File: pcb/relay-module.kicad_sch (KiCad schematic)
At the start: 57 parts, among them J1 AVR-UPDI-6, J2 QWICC, J3 Power In, J4 Power Out, K1 PR24-5V-900-1A, P1 MountingHole_Pad, P2 MountingHole_Pad, P3 MountingHole_Pad, P4 MountingHole_Pad, Q1 MMBT3904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

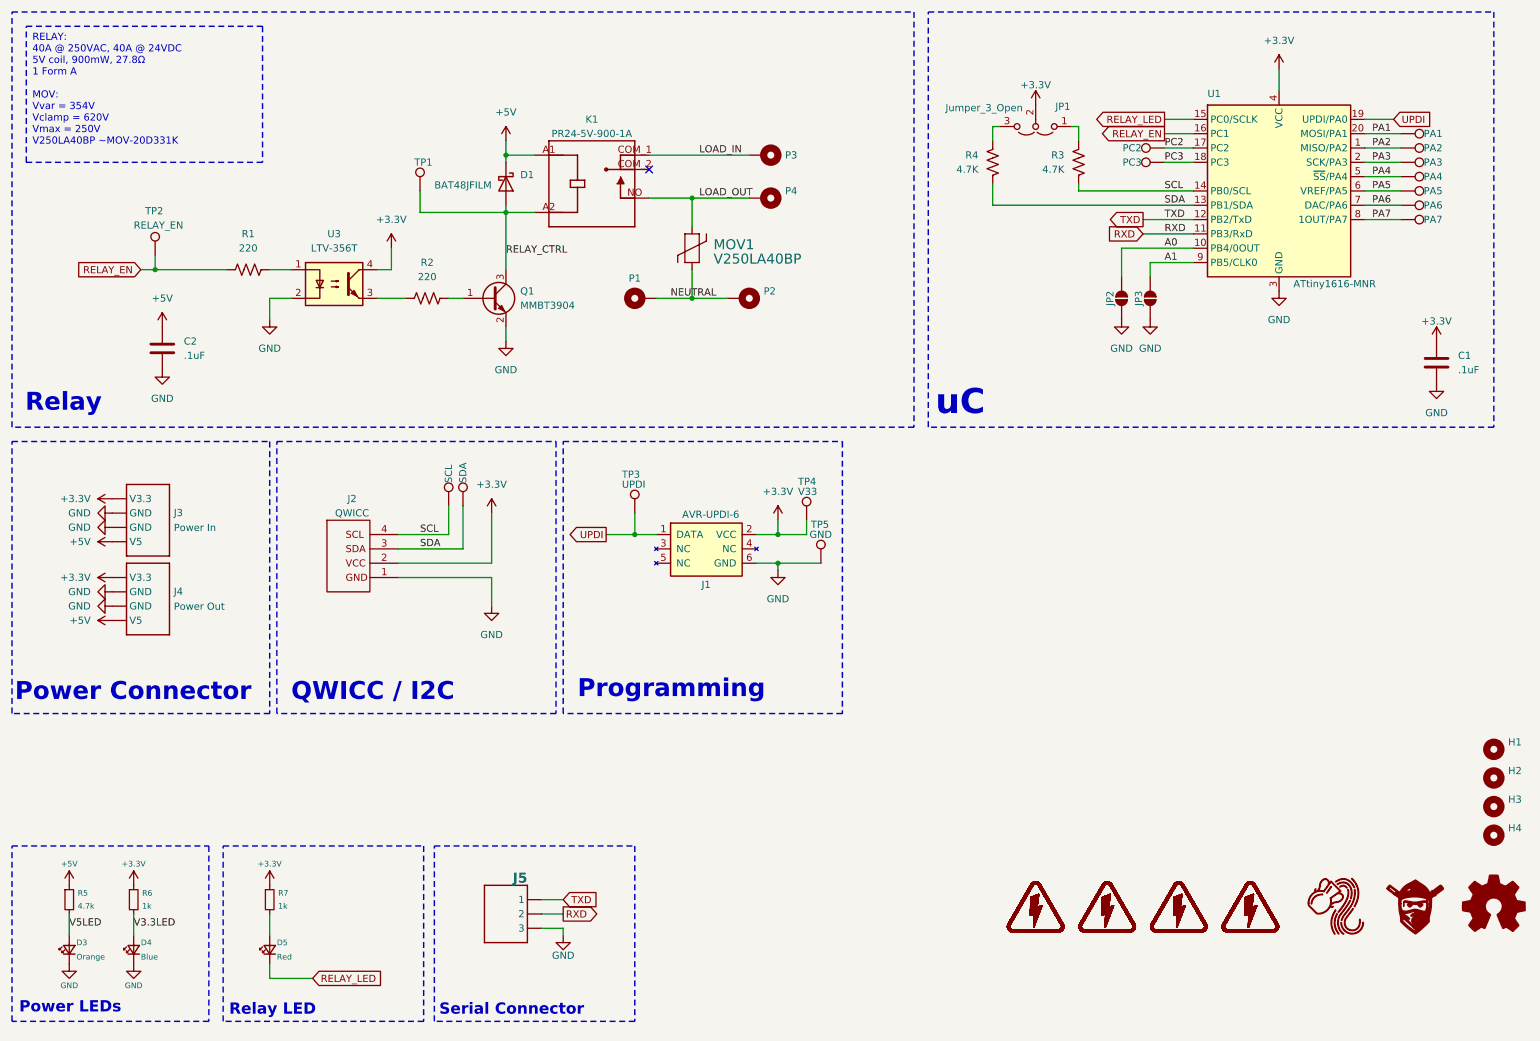
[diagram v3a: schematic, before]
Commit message: Changed to multi-sheet
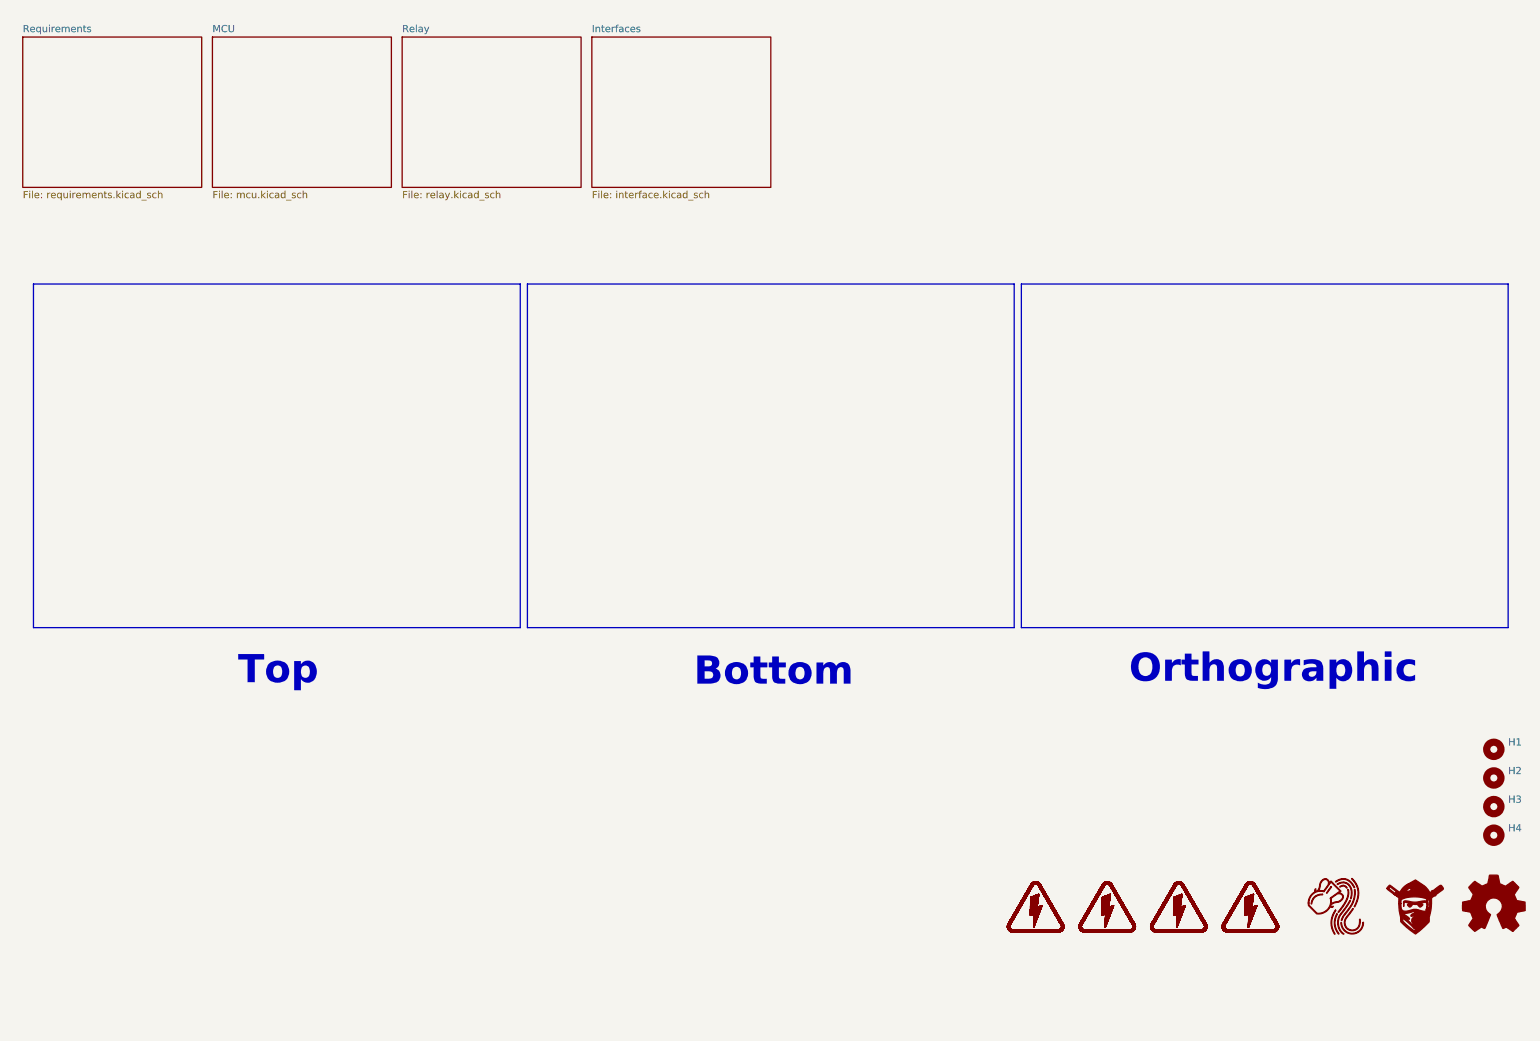
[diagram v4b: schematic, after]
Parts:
- removed C1, C2: .1uF, Capacitor_SMD:C_0603_1608Metric, symbol Device:C
- removed D1: BAT48JFILM, Diode_SMD:D_SOD-323, symbol Diode:BAT48JFILM
- removed D3: Orange, LED_SMD:LED_0603_1608Metric, symbol Device:LED_Small
- removed D4: Blue, LED_SMD:LED_0603_1608Metric, symbol Device:LED_Small
- removed D5: Red, LED_SMD:LED_0603_1608Metric, symbol Device:LED_Small
- removed J1: AVR-UPDI-6, CRGM Connector:PinHeader_2x03_P2.54mm_Vertical_SMD, symbol CRGM Connector:AVR-UPDI-6
- removed J2: QWICC, CRGM Connector:JST_SH_SM04B-SRSS-TB_1x04-1MP_P1.00mm_Horizontal, symbol CRGM Connector:QWIIC
- removed J3: Power In, CRGM Connector:JST_SH_SM04B-SRSS-TB_1x04-1MP_P1.00mm_Horizontal, symbol CRGM Connector:AQ_POWER
- removed J4: Power Out, CRGM Connector:JST_SH_SM04B-SRSS-TB_1x04-1MP_P1.00mm_Horizontal, symbol CRGM Connector:AQ_POWER
- removed J5: ~, Connector_JST:JST_SH_BM03B-SRSS-TB_1x03-1MP_P1.00mm_Vertical, symbol CRGM Connector:JST-SH-3
- removed JP1: Jumper_3_Open, CRGM Connector:SolderJumper-3_P1.3mm_Open_RoundedPad1.0x1.5mm, symbol Jumper:Jumper_3_Open
- removed JP2: A0, CRGM Connector:SolderJumper-2_P1.3mm_Open_RoundedPad1.0x1.5mm, symbol Jumper:SolderJumper_2_Open
- removed JP3: A1, CRGM Connector:SolderJumper-2_P1.3mm_Open_RoundedPad1.0x1.5mm, symbol Jumper:SolderJumper_2_Open
- removed K1: PR24-5V-900-1A, CRG Makes:RELAY_PR24-5V-900-1A, symbol CRG Makes:PR24-5V-900-1A
- removed MOV1: V250LA40BP, CRG Makes:V250LA40BP, symbol CRG Makes:MOV20D331K
- removed P1, P2, P3, P4: MountingHole_Pad, CRGM Mechanical:MountingHole_3.2mm_M3_ISO14580_Pad, symbol Mechanical:MountingHole_Pad
- removed Q1: MMBT3904, Package_TO_SOT_SMD:SOT-23, symbol Transistor_BJT:MMBT3904
- removed R1, R2: 220, Resistor_SMD:R_0603_1608Metric, symbol Device:R_US
- removed R3, R4: 4.7K, Resistor_SMD:R_0603_1608Metric, symbol Device:R_US
- removed R5: 4.7k, Resistor_SMD:R_0603_1608Metric, symbol Device:R_Small
- removed R6, R7: 1k, Resistor_SMD:R_0603_1608Metric, symbol Device:R_Small
- removed TP1: RELAY_CTRL, CRGM Mechanical:TestPoint_Pad_D1.0mm, symbol Connector:TestPoint
- removed TP10: PA3, CRGM Mechanical:TestPoint_Pad_D1.0mm, symbol Connector:TestPoint
- removed TP11: PA4, CRGM Mechanical:TestPoint_Pad_D1.0mm, symbol Connector:TestPoint
- removed TP12: PA5, CRGM Mechanical:TestPoint_Pad_D1.0mm, symbol Connector:TestPoint
- removed TP13: PA6, CRGM Mechanical:TestPoint_Pad_D1.0mm, symbol Connector:TestPoint
- removed TP14: PA7, CRGM Mechanical:TestPoint_Pad_D1.0mm, symbol Connector:TestPoint
- removed TP15: SCL, CRGM Mechanical:TestPoint_Pad_D1.0mm, symbol Connector:TestPoint
- removed TP16: SDA, CRGM Mechanical:TestPoint_Pad_D1.0mm, symbol Connector:TestPoint
- removed TP2: RELAY_EN, CRGM Mechanical:TestPoint_Pad_D1.0mm, symbol Connector:TestPoint
- removed TP3: UPDI, CRGM Mechanical:TestPoint_Pad_D1.0mm, symbol Connector:TestPoint
- removed TP4: V33, CRGM Mechanical:TestPoint_Pad_D1.0mm, symbol Connector:TestPoint
- removed TP5: GND, CRGM Mechanical:TestPoint_Pad_D1.0mm, symbol Connector:TestPoint
- removed TP6: PC2, CRGM Mechanical:TestPoint_Pad_D1.0mm, symbol Connector:TestPoint
- removed TP7: PC3, CRGM Mechanical:TestPoint_Pad_D1.0mm, symbol Connector:TestPoint
- removed TP8: PA1, CRGM Mechanical:TestPoint_Pad_D1.0mm, symbol Connector:TestPoint
- removed TP9: PA2, CRGM Mechanical:TestPoint_Pad_D1.0mm, symbol Connector:TestPoint
- removed U1: ATtiny1616-MNR, CRG Makes:VQFN-20-1EP_3x3mm_P0.4mm_EP1.7x1.7mm_ThermalVias, symbol CRG Makes:ATtiny1616-MNR
- removed U3: LTV-356T, Package_SO:SO-4_4.4x3.6mm_P2.54mm, symbol Isolator:LTV-356T
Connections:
- no-connect marks 1 -> 0
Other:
- added sheet Interfaces (interface.kicad_sch)
- added sheet MCU (mcu.kicad_sch)
- added sheet Relay (relay.kicad_sch)
- added sheet Requirements (requirements.kicad_sch)
- note added: "Bottom"
- note added: "Orthographic"
- note added: "Top"
- note removed: "Power Connector"
- note removed: "Power LEDs"
- note removed: "Programming"
- note removed: "QWICC / I2C"
- note removed: "Relay"
- note removed: "Relay LED"
- note removed: "Serial Connector"
- note removed: "uC"
